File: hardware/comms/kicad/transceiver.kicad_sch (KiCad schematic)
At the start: 0 parts

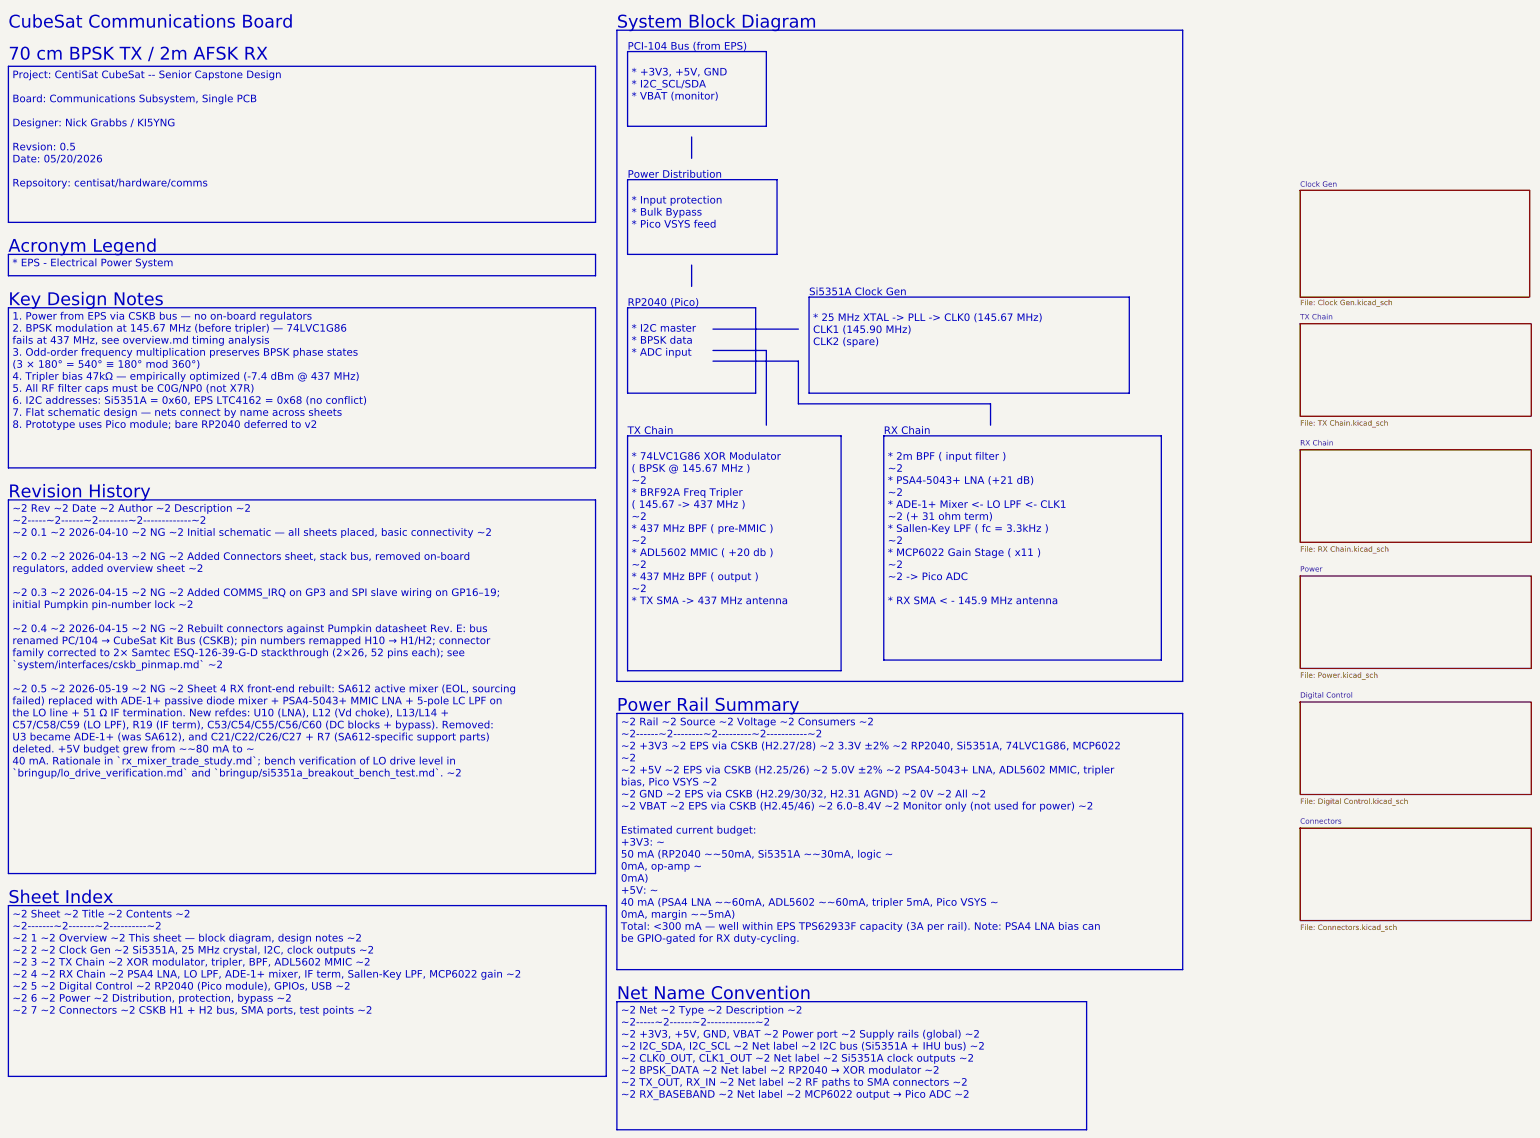
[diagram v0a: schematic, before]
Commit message: comms/kicad: rename project and sheets, correct schematic text
  Renames
  - transciever_kicad.{pro,sch,pcb} -> transceiver.{pro,sch,pcb}: the
    project name was misspelled, and the _kicad suffix was redundant
    inside a kicad/ directory.
  - Sheet files lose their spaces: Clock_Gen, Digital_Control, RX_Chain,
    TX_Chain. Sheetname keeps its space -- that is the label drawn on the
    sheet, not a path.
  - References updated in four places, not one: 4 Sheetfile properties in
    the root schematic, 186 per-symbol (project ...) instances across every
    sheet, 68 per-footprint (sheetfile ...) entries in the PCB, and
    meta.filename plus the root sheet name in the project file. Verified
    afterwards that all sheet references resolve, no sheet is orphaned, and
    the project file still parses.

  Spelling and stale labels
  - Title block: Revsion -> Revision, Repsoitory -> Repository, repository
    path centisat -> ember, project named EMBER.
  - PCI-104 -> CSKB in three files. PCI-104 is a different real standard,
    and the same sheet's own revision history records the bus being renamed
    to CSKB back at rev 0.4.
  - Status LED's -> Status LEDs; +20 db -> +20 dB; RX SMA < - -> <-.
  - The tripler note named BRF92A as the flight transistor: misspelled, and
    superseded by the 2SC3356 actually placed. Corrected to 2SC3356 with
    the MMBT3904-footprint note the implementation plan records. The
    ft=5 GHz figure is dropped rather than reassigned to a part it was not
    measured against.
  - Power sheet: the D4 forward-drop note referred to the SA612, replaced
    by the ADE-1+ back at rev 0.5. Now names the PSA4-5043+.
 Altium-to-KiCad text damage
  Three separate corruptions, classified before replacing so that real
  values were not caught up in it -- ~21 dB and ~20 dB both contain a
  literal ~2 and would have been mangled by a blind pass.
  - 144 table column separators rendered as literal ~2; now |, so the
    sheet index, rail summary, net c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
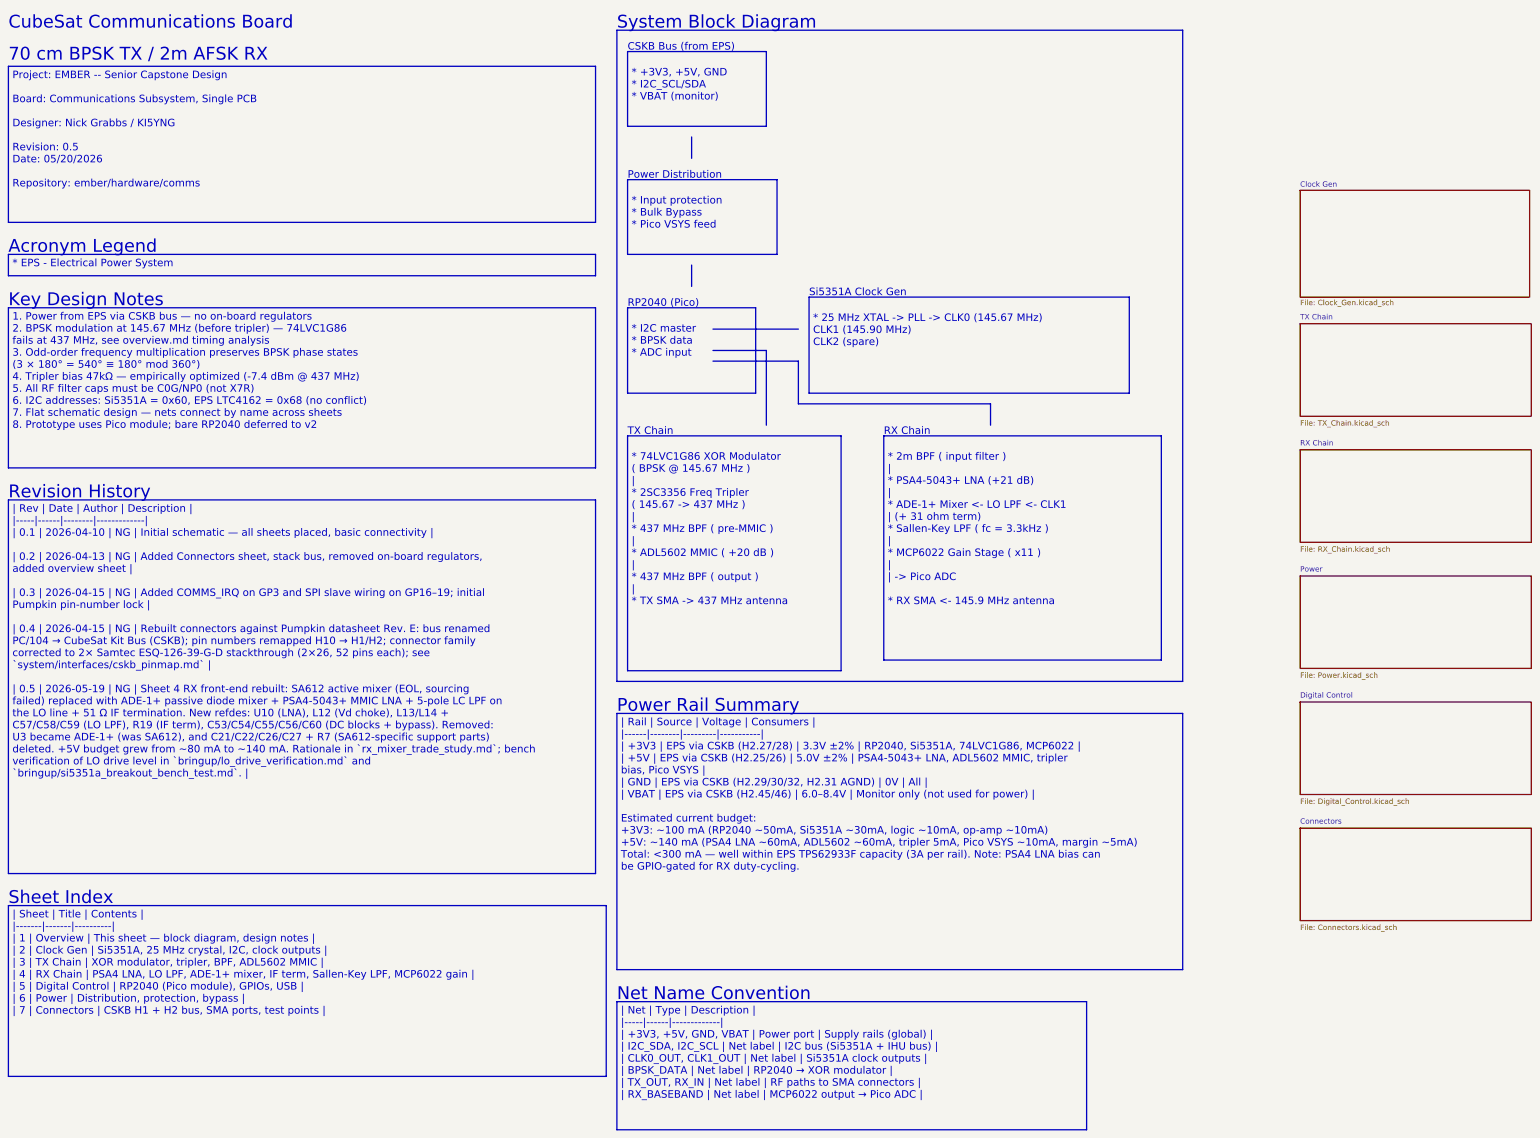
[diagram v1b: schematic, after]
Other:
- sheet Clock Gen: file Clock Gen.kicad_sch -> Clock_Gen.kicad_sch
- sheet Digital Control: file Digital Control.kicad_sch -> Digital_Control.kicad_sch
- sheet RX Chain: file RX Chain.kicad_sch -> RX_Chain.kicad_sch
- sheet TX Chain: file TX Chain.kicad_sch -> TX_Chain.kicad_sch
- note added: "CSKB Bus (from EPS)"
- note removed: "PCI-104 Bus (from EPS)"

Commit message: comms: checkpoint current KiCad design before ground station work
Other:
- added sheet Single Antenna RF Switch (RF_Switch.kicad_sch)
- title: CubeSat Comms -- Overview -> CubeSat Comms -- UHF/UHF Overview
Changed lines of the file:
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@@
 	(paper "A3")
 	(title_block
-		(title "CubeSat Comms -- Overview")
+		(title "CubeSat Comms -- UHF/UHF Overview")
 		(rev "A")
+		(comment 9 "UHF/UHF revision in review - not for fabrication")
 	)
 	(rectangle
@@
 			)
 		)
+	)
+	(sheet
+		(at 326.39 25.4)
+		(size 54.61 22.86)
+		(exclude_from_sim no)
+		(in_bom yes)
+		(on_board yes)
+		(dnp no)
+		(fields_autoplaced yes)
+		(stroke
+			(width 0.1524)
+			(type solid)
+		)
+		(fill
+			(color 0 0 0 0)
+		)
+		(property "Sheetname" "Single Antenna RF Switch"
+			(at 326.39 24.765 0)
+			(show_name no)
+			(do_not_autoplace no)
+			(effects
+				(font
+					(size 1.27 1.27)
+				)
+				(justify left bottom)
+			)
+		)
+		(property "Sheetfile" "RF_Switch.kicad_sch"
+			(at 326.39 48.895 0)
+			(show_name no)
+			(do_not_autoplace no)
+			(effects
+				(font
+					(size 1.27 1.27)
+				)
+				(justify left top)
+			)
+		)

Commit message: Complete dual-CAN transceiver hardware prototype
Preserve the current transceiver schematics, PCB, libraries and validation evidence as a focused hardware review against main.
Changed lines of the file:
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@@
 	(text_box "\n * 74LVC1G86 XOR Modulator\n    ( BPSK @ 145.67 MHz )\n                    |\n * 2SC3356 Freq Tripler\n    ( 145.67 -> 437 MHz )\n                    |\n * 437 MHz BPF ( pre-MMIC )\n                    |\n * ADL5602 MMIC ( +20 dB )\n                    |\n * 437 MHz BPF ( output )\n                    |\n * TX SMA -> 437 MHz antenna"
 		(exclude_from_sim no)
-		(at 217.17 116.84 0)
-		(size -50.8 55.88)
+		(at 166.37 116.84 0)
+		(size 50.8 55.88)
 		(margins 0.9525 0.9525 0.9525 0.9525)
 		(stroke
